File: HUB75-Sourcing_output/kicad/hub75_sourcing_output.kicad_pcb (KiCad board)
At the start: 2 copper layers, 85 x 56 mm, 114 parts, among them J1 Conn_01x02_Male, J10 Conn_01x02_Male, J11 Conn_01x02_Male, J12 Conn_01x02_Male, J13 Screw_Terminal_01x02, J2 Conn_01x02_Male, J3 Conn_01x02_Male, J4 Conn_01x02_Male, J5 Conn_01x02_Male, J6 Conn_01x02_Male, J7 Conn_01x02_Male, J8 Conn_01x02_Male, J9 Conn_01x02_Male, Q1 BSS84, Q10 BSS84, Q11 BSS84, Q12 BSS84, Q13 AO3401A, Q2 BSS84, Q3 BSS84, Q4 BSS84, Q5 BSS84, Q6 BSS84, Q7 BSS84, Q8 BSS84, Q9 BSS84, U1 LTV-827, U10 LTV-827, U11 NSI45020AT1G, U12 NSI45020AT1G, U13 LTV-827, U14 NSI45020AT1G, U15 NSI45020AT1G, U16 LTV-827, U17 NSI45020AT1G, U18 NSI45020AT1G, U2 NSI45020AT1G, U3 NSI45020AT1G, U4 LTV-827, U5 NSI45020AT1G, U6 NSI45020AT1G, U7 LTV-827, U8 NSI45020AT1G, U9 NSI45020AT1G

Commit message: Proto-type production ready
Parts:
- moved U2 0.34 mm to (57.1, 90.9)
- moved U3 0.34 mm to (57.1, 88.4)
- moved U5 0.34 mm to (69.4, 90.9)
- moved U6 0.34 mm to (69.4, 88.4)
- moved U8 0.34 mm to (81.6, 90.9)
- moved U9 0.34 mm to (81.6, 88.4)
- moved U17 0.33 mm to (118.8, 90.9)
- moved U18 0.33 mm to (118.8, 88.4)
- moved U11 0.32 mm to (93.9, 90.9)
- moved U12 0.32 mm to (93.9, 88.4)
- moved U14 0.32 mm to (106.4, 90.9)
- moved U15 0.32 mm to (106.4, 88.4)
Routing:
- net Net-(D8-Pad2): track 17.6 -> 12.2 mm
- net Net-(D20-Pad2): track 17.6 -> 12.2 mm
- net Net-(D16-Pad2): track 17.6 -> 12.2 mm
- net Net-(D12-Pad2): track 17.6 -> 12.2 mm
- net Net-(D4-Pad2): track 17.6 -> 12.2 mm
- net Net-(D24-Pad2): track 17.6 -> 12.2 mm

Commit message: Moved license logo + added name
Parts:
- moved G*** 14.0 mm to (131.6, 64.3), turned to 90 degrees
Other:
- board text added: "By Peter van Tol"
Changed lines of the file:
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@@
   )
   (footprint "LOGO" (layer "B.Cu")
-    (at 121.158 54.864 180)
+    (at 131.572 64.262 90)
     (attr board_only exclude_from_pos_files exclude_from_bom)
-    (fp_text reference "G***" (at 0 0) (layer "B.SilkS") hide
+    (fp_text reference "G***" (at 0 0 90) (layer "B.SilkS") hide
       (effects (font (size 1.524 1.524) (thickness 0.3)) (justify mirror))
     )
-    (fp_text value "LOGO" (at 0.75 0) (layer "B.SilkS") hide
+    (fp_text value "LOGO" (at 0.75 0 90) (layer "B.SilkS") hide
       (effects (font (size 1.524 1.524) (thickness 0.3)) (justify mirror))
     )
@@
   )
   (gr_rect (start 51.054 50.546) (end 136.054 106.546) (layer "Edge.Cuts") (width 0.1) (fill none))
+  (gr_text "By Peter van Tol" (at 127.762 64.262 270) (layer "B.SilkS")
+    (effects (font (size 1 1) (thickness 0.25)) (justify mirror))
+  )
   (gr_text "+5~24V\nFIELD\nPOWER" (at 130.522 80.694 90) (layer "F.SilkS")
     (effects (font (size 1.524 1.524) (thickness 0.3048)))
@@
     )
   )
+  (group "" (id 9a6c9f54-b9ec-4497-a7bb-ddbac72eb8a6)
+    (members
+      9b3192ea-dfad-489e-b027-2f544de25025
+      c680adfa-05ab-4e3b-a1f5-cad651745774
+    )
+  )

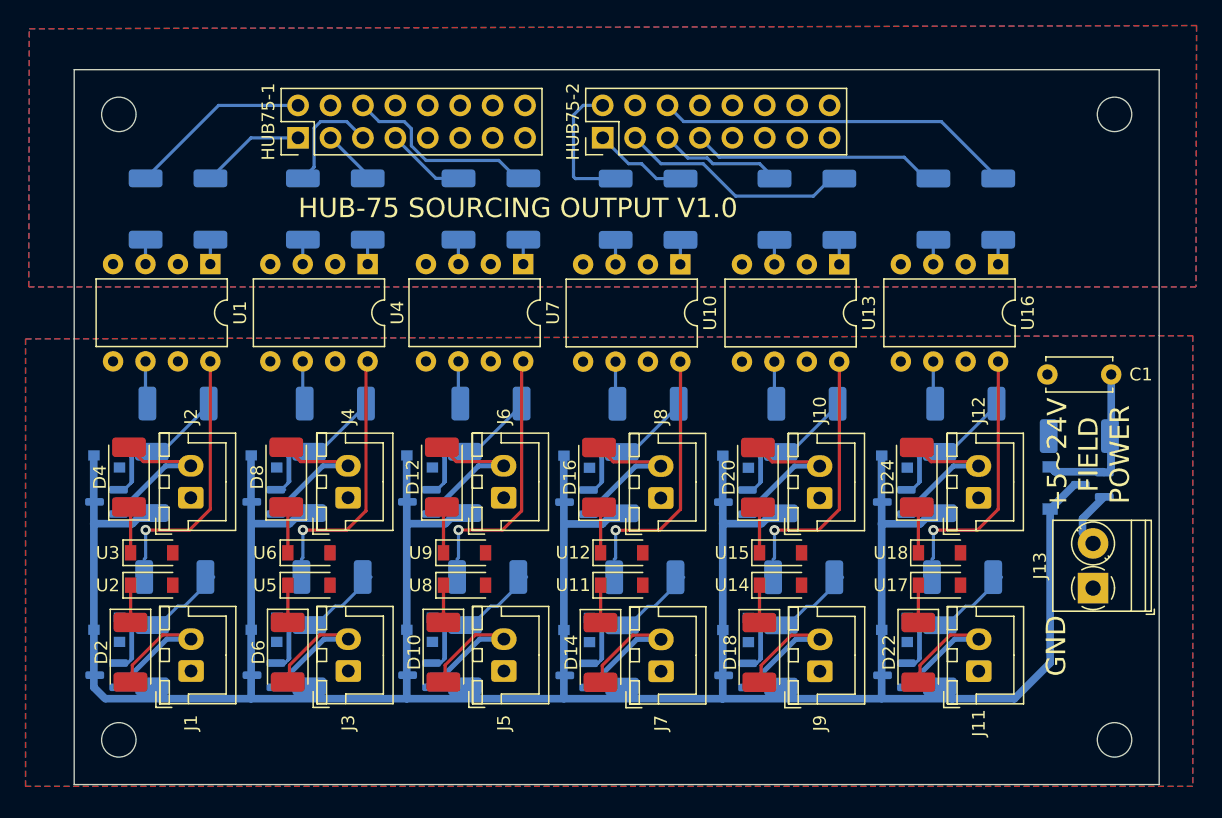
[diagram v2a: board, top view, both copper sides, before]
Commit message: Update board with current mirror + backup
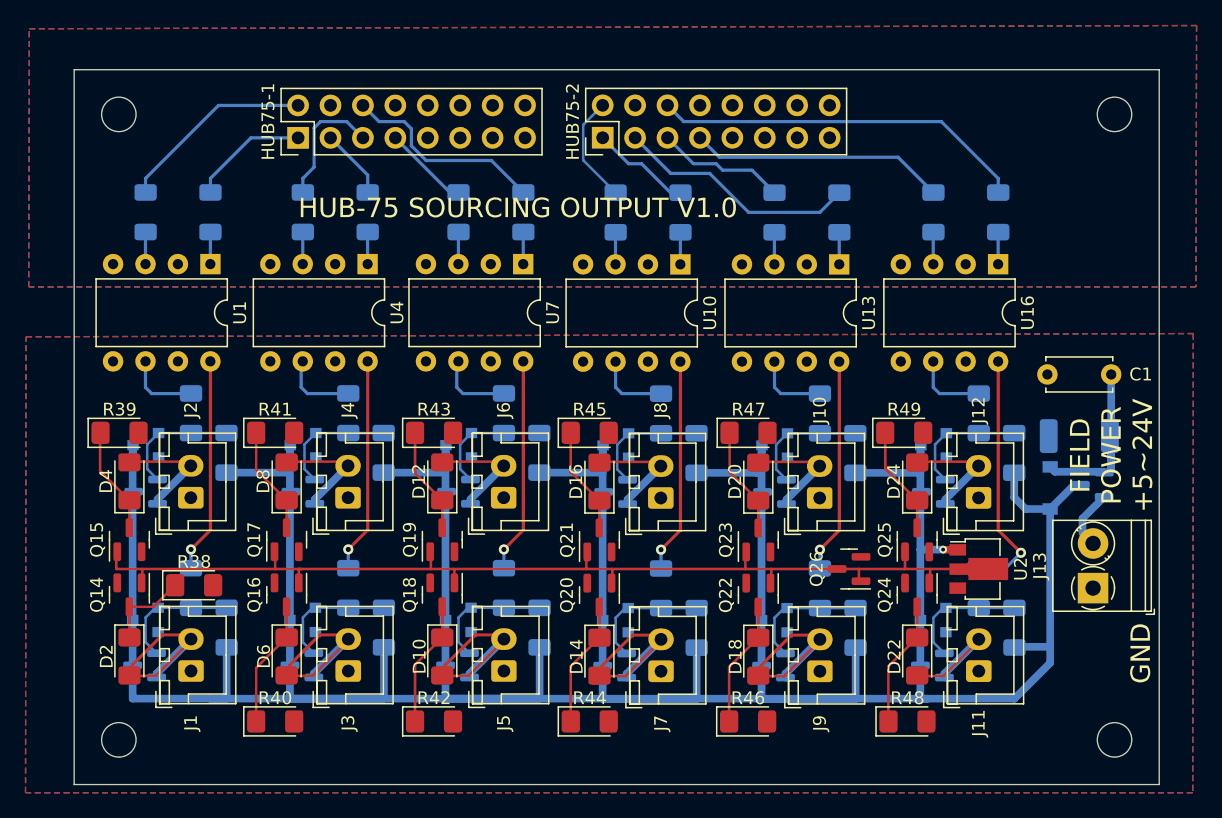
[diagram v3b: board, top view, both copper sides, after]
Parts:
- removed U11, U12, U14, U15, U17, U18, U3, U5, U6, U8, U9: NSI45020AT1G, Diode_SMD:D_SOD-123
- added Q14: 2N7002, Package_TO_SOT_SMD:SOT-23, F.Cu at (55.4, 91.7)
- added Q15: 2N7002, Package_TO_SOT_SMD:SOT-23, F.Cu at (55.4, 87.4)
- added Q16: 2N7002, Package_TO_SOT_SMD:SOT-23, F.Cu at (67.7, 91.7)
- added Q17: 2N7002, Package_TO_SOT_SMD:SOT-23, F.Cu at (67.7, 87.4)
- added Q18: 2N7002, Package_TO_SOT_SMD:SOT-23, F.Cu at (79.9, 91.7)
- added Q19: 2N7002, Package_TO_SOT_SMD:SOT-23, F.Cu at (79.9, 87.4)
- added Q20: 2N7002, Package_TO_SOT_SMD:SOT-23, F.Cu at (92.2, 91.7)
- added Q21: 2N7002, Package_TO_SOT_SMD:SOT-23, F.Cu at (92.2, 87.4)
- added Q22: 2N7002, Package_TO_SOT_SMD:SOT-23, F.Cu at (104.6, 91.7)
- added Q23: 2N7002, Package_TO_SOT_SMD:SOT-23, F.Cu at (104.6, 87.4)
- added Q24: 2N7002, Package_TO_SOT_SMD:SOT-23, F.Cu at (117.1, 91.7)
- added Q25: 2N7002, Package_TO_SOT_SMD:SOT-23, F.Cu at (117.1, 87.4)
- added Q26: 2N7002, Package_TO_SOT_SMD:SOT-23, F.Cu at (111.8, 89.7)
- added R38: R, LED_SMD:LED_1206_3216Metric_Pad1.42x1.75mm_HandSolder, F.Cu at (60.5, 90.9)
- added R39: R, LED_SMD:LED_1206_3216Metric_Pad1.42x1.75mm_HandSolder, F.Cu at (54.6, 79.0)
- added R40: R, LED_SMD:LED_1206_3216Metric_Pad1.42x1.75mm_HandSolder, F.Cu at (66.8, 101.6)
- added R41: R, LED_SMD:LED_1206_3216Metric_Pad1.42x1.75mm_HandSolder, F.Cu at (66.8, 79.0)
- added R42: R, LED_SMD:LED_1206_3216Metric_Pad1.42x1.75mm_HandSolder, F.Cu at (79.2, 101.6)
- added R43: R, LED_SMD:LED_1206_3216Metric_Pad1.42x1.75mm_HandSolder, F.Cu at (79.2, 79.0)
- added R44: R, LED_SMD:LED_1206_3216Metric_Pad1.42x1.75mm_HandSolder, F.Cu at (91.4, 101.6)
- added R45: R, LED_SMD:LED_1206_3216Metric_Pad1.42x1.75mm_HandSolder, F.Cu at (91.4, 79.0)
- added R46: R, LED_SMD:LED_1206_3216Metric_Pad1.42x1.75mm_HandSolder, F.Cu at (103.8, 101.6)
- added R47: R, LED_SMD:LED_1206_3216Metric_Pad1.42x1.75mm_HandSolder, F.Cu at (103.9, 79.0)
- added R48: R, LED_SMD:LED_1206_3216Metric_Pad1.42x1.75mm_HandSolder, F.Cu at (116.3, 101.6)
- added R49: R, LED_SMD:LED_1206_3216Metric_Pad1.42x1.75mm_HandSolder, F.Cu at (116.1, 79.0)
- D10, D12, D14, D16, D18, D2, D20, D22, D24, D4, D6, D8: footprint LED_SMD:LED_2010_5025Metric_Pad1.52x2.65mm_HandSolder -> LED_SMD:LED_1206_3216Metric_Pad1.42x1.75mm_HandSolder
- R1, R10, R11, R12, R13, R14, R15, R16, R17, R18, R19, R2, R20, R21, R22, R23, R24, R25, R26, R27, R28, R29, R3, R30, R31, R32, R33, R34, R35, R36, R4, R5, R6, R7, R8, R9: footprint Resistor_SMD:R_2010_5025Metric_Pad1.40x2.65mm_HandSolder -> Resistor_SMD:R_1206_3216Metric_Pad1.30x1.75mm_HandSolder
- U2: value NSI45020AT1G -> HV9921N8-G; footprint Diode_SMD:D_SOD-123 -> Package_TO_SOT_SMD:SOT-89-3
- moved U2 64.8 mm to (121.9, 89.7)
- moved R24 6.29 mm to (99.8, 80.6)
- moved R36 6.29 mm to (124.7, 80.6)
- moved R12 6.29 mm to (75.3, 80.6)
- moved R18 6.29 mm to (87.5, 80.6)
- moved R30 6.29 mm to (112.3, 80.6)
- moved R6 6.29 mm to (63.0, 80.6)
- moved R4 6.24 mm to (63.0, 94.2)
- moved R10 6.24 mm to (75.3, 94.2)
- moved R16 6.24 mm to (87.5, 94.2)
- moved R22 6.24 mm to (99.8, 94.3)
- moved R28 6.24 mm to (112.3, 94.3)
- moved R34 6.24 mm to (124.7, 94.3)
- moved D11 3.17 mm to (81.2, 80.0)
- moved Q6 3.17 mm to (81.2, 83.6)
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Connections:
- U2 pad 1: Net-(D2-Pad1) -> VDD
- U2 pad 2: GNDD -> CUR_MIRROR
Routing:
- net VDD: track 382.9 -> 290.4 mm, vias 0 -> 1
- net CUR_MIRROR: track 0.00 -> 82.2 mm
- net Net-(D7-Pad2): track 17.4 -> 9.54 mm
- net Net-(D11-Pad2): track 16.6 -> 9.54 mm
- net Net-(D3-Pad2): track 16.6 -> 9.54 mm
- net Net-(D15-Pad2): track 16.6 -> 9.54 mm
- net Net-(D23-Pad2): track 16.6 -> 9.54 mm
- net Net-(D19-Pad2): track 16.6 -> 9.54 mm
- net Net-(D6-Pad1): track 3.12 -> 9.64 mm
- net Net-(D18-Pad1): track 3.12 -> 9.57 mm
- net Net-(D22-Pad1): track 3.12 -> 9.57 mm
- net Net-(D14-Pad1): track 3.12 -> 9.56 mm
- net Net-(D10-Pad1): track 3.12 -> 9.53 mm
- net Net-(D24-Pad1): track 3.12 -> 8.48 mm
- net Net-(D8-Pad1): track 3.12 -> 8.42 mm
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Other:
- board text added: "FIELD POWER +5~24V"
- board text removed: "+5~24V FIELD POWER"

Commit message: Regenerated
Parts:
- U2: value HV9921N8-G -> CL2N8-G
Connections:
- HUB75-1 pad 8: GND -> unconnected-(HUB75-1-Pad8)
- HUB75-2 pad 8: GND -> unconnected-(HUB75-2-Pad8)
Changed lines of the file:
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@@
   (net 97 "Net-(D1-Pad2)")
   (net 98 "CUR_MIRROR")
+  (net 99 "unconnected-(HUB75-1-Pad8)")
+  (net 100 "unconnected-(HUB75-2-Pad8)")
   (footprint "Connector_JST:JST_XH_B2B-XH-A_1x02_P2.50mm_Vertical" (layer "F.Cu")
     (at 109.474 97.673 90)
@@
     (property "Sheetfile" "FET-driver.kicad_sch")
     (property "Sheetname" "FET-driver1")
+    (property "exclude_from_bom" "")
     (attr smd exclude_from_pos_files exclude_from_bom)
     (fp_text reference "R40" (at 0 -1.82) (layer "F.SilkS")
@@
     (property "Sheetfile" "FET-driver.kicad_sch")
     (property "Sheetname" "FET-driver2")
+    (property "exclude_from_bom" "")
     (attr smd exclude_from_pos_files exclude_from_bom)
     (fp_text reference "R39" (at 0 -1.82) (layer "F.SilkS")
@@
     (property "Sheetfile" "FET-driver.kicad_sch")
     (property "Sheetname" "FET-driver1")
+    (property "exclude_from_bom" "")
     (attr smd exclude_from_pos_files exclude_from_bom)
     (fp_text reference "R38" (at 0 -1.82) (layer "F.SilkS")
@@
     (property "Sheetfile" "FET-driver.kicad_sch")
     (property "Sheetname" "FET-driver2")
+    (property "exclude_from_bom" "")
     (attr smd exclude_from_pos_files exclude_from_bom)
     (fp_text reference "R47" (at 0 -1.82) (layer "F.SilkS")
@@
     (property "Sheetfile" "FET-driver.kicad_sch")
     (property "Sheetname" "FET-driver1")
+    (property "exclude_from_bom" "")
     (attr smd exclude_from_pos_files exclude_from_bom)
     (fp_text reference "R48" (at 0 -1.82) (layer "F.SilkS")
@@
     (property "Sheetfile" "FET-driver.kicad_sch")
     (property "Sheetname" "FET-driver2")
+    (property "exclude_from_bom" "")
     (attr smd exclude_from_pos_files exclude_from_bom)
     (fp_text reference "R41" (at 0 -1.82) (layer "F.SilkS")
@@
       (net 16 "GPIO1-6") (pinfunction "Pin_7") (pintype "passive"))
     (pad "8" thru_hole oval (at 2.54 7.62 90) (size 1.7 1.7) (drill 1) (layers *.Cu *.Mask)
-      (net 4 "GND") (pinfunction "Pin_8") (pintype "passive"))
+      (net 99 "unconnected-(HUB75-1-Pad8)") (pinfunction "Pin_8") (pintype "passive"))
     (pad "9" thru_hole oval (at 0 10.16 90) (size 1.7 1.7) (drill 1) (layers *.Cu *.Mask)
       (net 61 "unconnected-(HUB75-1-Pad9)") (pinfunction "Pin_9") (pintype "passive"))
@@
     (property "Sheetfile" "FET-driver.kicad_sch")
     (property "Sheetname" "FET-driver2")
+    (property "exclude_from_bom" "")
     (attr smd exclude_from_pos_files exclude_from_bom)
     (fp_text reference "R49" (at 0 -1.82) (layer "F.SilkS")
@@
       (effects (font (size 1 1) (thickness 0.15)))
     )
-    (fp_text value "HV9921N8-G" (at 0.3 3.5) (layer "F.Fab") hide
+    (fp_text value "CL2N8-G" (at 0.3 3.5) (layer "F.Fab") hide
       (effects (font (size 1 1) (thickness 0.15)))
     )
@@
       (net 26 "GPIO2-6") (pinfunction "Pin_7") (pintype "passive"))
     (pad "8" thru_hole oval (at 2.54 7.62 90) (size 1.7 1.7) (drill 1) (layers *.Cu *.Mask)
-      (net 4 "GND") (pinfunction "Pin_8") (pintype "passive"))
+      (net 100 "unconnected-(HUB75-2-Pad8)") (pinfunction "Pin_8") (pintype "passive"))
     (pad "9" thru_hole oval (at 0 10.16 90) (size 1.7 1.7) (drill 1) (layers *.Cu *.Mask)
       (net 47 "unconnected-(HUB75-2-Pad9)") (pinfunction "Pin_9") (pintype "passive"))
@@
     (property "Sheetfile" "FET-driver.kicad_sch")
     (property "Sheetname" "FET-driver1")
+    (property "exclude_from_bom" "")
     (attr smd exclude_from_pos_files exclude_from_bom)
     (fp_text reference "R44" (at 0 -1.82) (layer "F.SilkS")
@@
     (property "Sheetfile" "FET-driver.kicad_sch")
     (property "Sheetname" "FET-driver1")
+    (property "exclude_from_bom" "")
     (attr smd exclude_from_pos_files exclude_from_bom)
     (fp_text reference "R42" (at 0 -1.82) (layer "F.SilkS")
@@
     (property "Sheetfile" "FET-driver.kicad_sch")
     (property "Sheetname" "FET-driver2")
+    (property "exclude_from_bom" "")
     (attr smd exclude_from_pos_files exclude_from_bom)
     (fp_text reference "R45" (at 0 -1.82) (layer "F.SilkS")
@@
     (property "Sheetfile" "FET-driver.kicad_sch")
     (property "Sheetname" "FET-driver2")
+    (property "exclude_from_bom" "")
     (attr smd exclude_from_pos_files exclude_from_bom)
     (fp_text reference "R43" (at 0 -1.82) (layer "F.SilkS")
@@
     (property "Sheetfile" "FET-driver.kicad_sch")
     (property "Sheetname" "FET-driver1")
+    (property "exclude_from_bom" "")
     (attr smd exclude_from_pos_files exclude_from_bom)
     (fp_text reference "R46" (at 0 -1.82) (layer "F.SilkS")

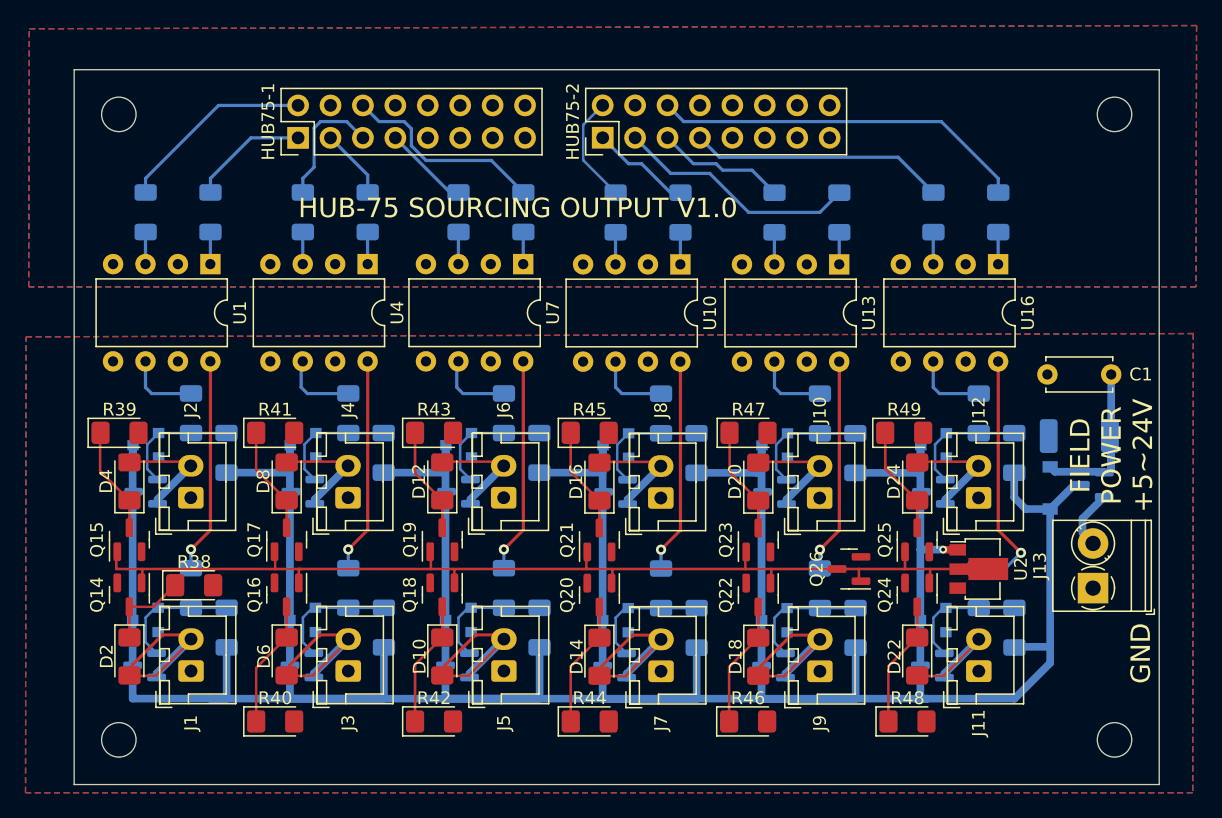
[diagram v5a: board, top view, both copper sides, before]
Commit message: New version after prototype failed
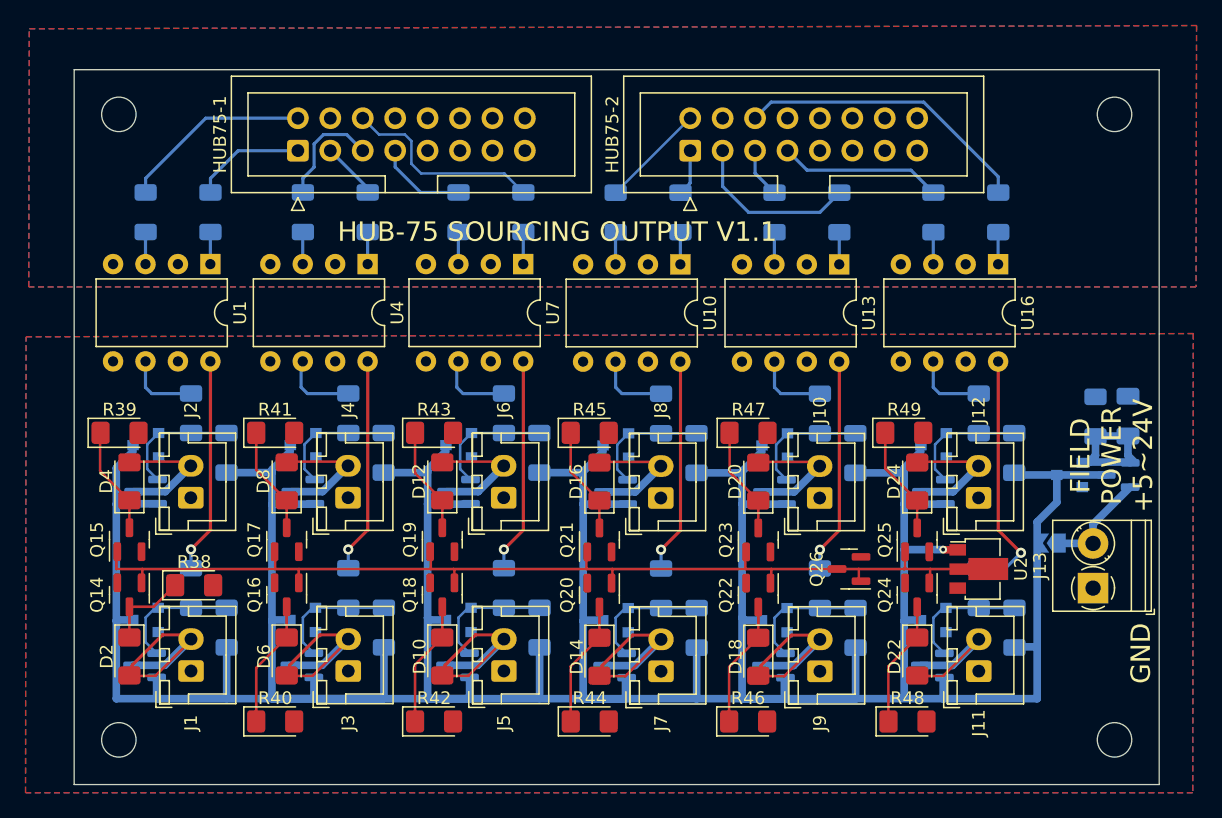
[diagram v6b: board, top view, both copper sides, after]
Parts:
- added JP1: Jumper_2_Open, Jumper:SolderJumper-2_P1.3mm_Open_TrianglePad1.0x1.5mm, B.Cu at (127.5, 87.6)
- C1: footprint Capacitor_THT:C_Disc_D5.0mm_W2.5mm_P5.00mm -> Capacitor_SMD:C_1206_3216Metric_Pad1.33x1.80mm_HandSolder; moved to B.Cu
- D25: footprint Diode_SMD:D_SOD-123 -> Diode_SMD:D_SOT-23_ANK
- HUB75-1, HUB75-2: footprint Connector_PinHeader_2.54mm:PinHeader_2x08_P2.54mm_Vertical -> Connector_IDC:IDC-Header_2x08_P2.54mm_Vertical
- R37: footprint Resistor_SMD:R_2010_5025Metric_Pad1.40x2.65mm_HandSolder -> Resistor_SMD:R_1206_3216Metric_Pad1.30x1.75mm_HandSolder
- moved HUB75-2 6.93 mm to (99.3, 56.9)
- moved C1 3.52 mm to (133.6, 77.7), turned to 90 degrees
- moved Q13 2.17 mm to (132.8, 82.3)
- moved R37 1.98 mm to (131.1, 77.7), turned to 90 degrees
- moved D25 1.83 mm to (129.0, 82.3), turned to 180 degrees
- moved HUB75-1 1.00 mm to (68.6, 56.9)
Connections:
- Q1 pad 2: Net-(D2-Pad2) -> VDD
- Q1 pad 3: VDD -> Net-(D2-Pad2)
- Q10 pad 2: Net-(D20-Pad2) -> VDD
- Q10 pad 3: VDD -> Net-(D20-Pad2)
- Q11 pad 2: Net-(D22-Pad2) -> VDD
- Q11 pad 3: VDD -> Net-(D22-Pad2)
- Q12 pad 2: Net-(D24-Pad2) -> VDD
- Q12 pad 3: VDD -> Net-(D24-Pad2)
- Q2 pad 2: Net-(D4-Pad2) -> VDD
- Q2 pad 3: VDD -> Net-(D4-Pad2)
- Q3 pad 2: Net-(D6-Pad2) -> VDD
- Q3 pad 3: VDD -> Net-(D6-Pad2)
- Q4 pad 2: Net-(D8-Pad2) -> VDD
- Q4 pad 3: VDD -> Net-(D8-Pad2)
- Q5 pad 2: Net-(D10-Pad2) -> VDD
- Q5 pad 3: VDD -> Net-(D10-Pad2)
- Q6 pad 2: Net-(D12-Pad2) -> VDD
- Q6 pad 3: VDD -> Net-(D12-Pad2)
- Q7 pad 2: Net-(D14-Pad2) -> VDD
- Q7 pad 3: VDD -> Net-(D14-Pad2)
- Q8 pad 2: Net-(D16-Pad2) -> VDD
- Q8 pad 3: VDD -> Net-(D16-Pad2)
- Q9 pad 2: Net-(D18-Pad2) -> VDD
- Q9 pad 3: VDD -> Net-(D18-Pad2)
- U1 pad 5: unconnected-(U1-Pad5) -> GNDD
- U10 pad 5: unconnected-(U10-Pad5) -> GNDD
- U13 pad 5: unconnected-(U13-Pad5) -> GNDD
- U16 pad 5: unconnected-(U16-Pad5) -> GNDD
- U4 pad 5: unconnected-(U4-Pad5) -> GNDD
- U7 pad 5: unconnected-(U7-Pad5) -> GNDD
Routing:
- net VDD: track 290.4 -> 323.9 mm
- net GPIO2-6: track 20.1 -> 12.8 mm
- net GPIO2-4: track 10.2 -> 3.93 mm
- net GPIO2-5: track 29.4 -> 23.2 mm
- net GPIO2-3: track 18.8 -> 13.2 mm
- net GPIO2-1: track 7.88 -> 3.61 mm
- net Net-(J13-Pad2): track 4.70 -> 8.27 mm
- net Net-(C1-Pad1): track 14.8 -> 11.4 mm
- net Net-(D22-Pad2): track 9.82 -> 11.1 mm
- net Net-(D18-Pad2): track 16.4 -> 17.7 mm
- net Net-(D6-Pad2): track 16.4 -> 17.7 mm
- net Net-(D14-Pad2): track 16.4 -> 17.7 mm
- net Net-(D2-Pad2): track 16.4 -> 17.7 mm
- net Net-(D10-Pad2): track 16.4 -> 17.7 mm
- net Net-(D20-Pad2): track 8.60 -> 9.87 mm
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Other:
- board text added: "HUB-75 SOURCING OUTPUT V1.1"
- board text removed: "HUB-75 SOURCING OUTPUT V1.0"
